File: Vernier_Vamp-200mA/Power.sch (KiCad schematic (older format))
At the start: 69 parts, among them J4 Conn_02x07_Odd_Even, Q1 Si4447ADY, Q2 IRF8707PbF, SW1 DPDT_Hirose, U1 LM4040DBZ-5, U2 LM4040DBZ-5, U3 LM393, U4 TPS7A470x, U5 TPS7A470x, U6 TPS7A33

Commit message: Coil driver version 1.0B
Updated coil driver 200mA version with fixes requested by Iain.
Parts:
- removed C56, C57, C58, C59, C62, C63: 100n, Capacitor_SMD:C_0603_1608Metric_Pad1.05x0.95mm_HandSolder, symbol Device:C_Small
- removed D3, D4, D5, D6: SMBJ16A, Diode_SMD:D_SMB_Handsoldering, symbol SMBJ15A:SMBJ15A
- removed F1, F2: 1A, Fuse:Fuse_1812_4532Metric_Pad1.30x3.40mm_HandSolder, symbol Device:Polyfuse_Small
- removed H1, H2, H3, H4, H5: MountingHole_Pad, MountingHole:MountingHole_3.2mm_M3_Pad_Via, symbol Mechanical:MountingHole_Pad
- removed J4: Conn_02x07_Odd_Even, Connector_Hirose:Hirose_DF11-14DP-2DSA_2x07_P2.00mm_Vertical, symbol Connector_Generic:Conn_02x07_Odd_Even
- removed Q1: Si4447ADY, Package_SO:SO-8_3.9x4.9mm_P1.27mm, symbol Si4447ADY:Si4447ADY
- removed Q2: IRF8707PbF, Package_SO:SO-8_3.9x4.9mm_P1.27mm, symbol IRF8707PbF:IRF8707PbF
- removed R1, R11, R12, R15, R16, R17, R2, R3, R4, R5, R6: 10k, Resistor_SMD:R_0603_1608Metric_Pad1.05x0.95mm_HandSolder, symbol Device:R_Small
- removed R10, R8: 100k, Resistor_SMD:R_0603_1608Metric_Pad1.05x0.95mm_HandSolder, symbol Device:R_Small
- removed R7, R9: 120k, Resistor_SMD:R_0603_1608Metric_Pad1.05x0.95mm_HandSolder, symbol Device:R_Small
- removed SW1: DPDT_Hirose, Connector_Hirose:Hirose_DF11-6DP-2DSA_2x03_P2.00mm_Vertical, symbol SW_DPDT_Hirose:DPDT_Hirose
- removed TP1, TP10, TP11, TP2, TP3, TP4, TP5, TP6, TP7, TP8, TP9: TestPoint_Probe, TestPoint:TestPoint_Pad_D1.0mm, symbol Connector:TestPoint_Probe
- removed U1, U2: LM4040DBZ-5, Package_TO_SOT_SMD:SOT-23, symbol Reference_Voltage:LM4040DBZ-5
- removed U3: LM393, Package_SO:TSSOP-8_4.4x3mm_P0.65mm, symbol Comparator:LM393
- U4, U5: symbol TPS74A4700:TPS7A470x -> TPS74A4700:TPS7A4700
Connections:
- net labels added: +7.5V, -7.5V
- net labels removed: +5VD, +5V_c_ref, +8V, +BATT, -5V_c_ref, -8V, -BATT, LED1_N, LED1_P, LED2_N, LED2_P, LED3_N, LED3_P, LED4_N, LED4_P, LED5_N, LED5_P, LED6_N, LED6_P, LED7_N, LED7_P
- wire segments 254 -> 100
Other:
- note added: "Ultra low noise LDO, configured to provide +7.5VDC"
- note added: "Ultra low noise LDO, configured to provide\n -7.5VDC\nComplementary pair to TPS7A470x"
- note removed: "Extra redundancy passive protection\nLimits the supply to 16.7V\nUses PPTC as a resetable fuse"
- note removed: "Low battery indicator (< 11V)\n"
- note removed: "Panel LED\nconnector"
- note removed: "Positive/Negative active protection\ncircuit\nTVS used to limit GS voltage\nalso used for ESD protection"
- note removed: "Power good\nindicators"
- note removed: "Reverse polarity protection\n"
- note removed: "Soft On/Off DPDT switch\n"
- note removed: "Ultra low noise LDO, configured to provide +7.5VDC (ignore +8V label)"
- note removed: "Ultra low noise LDO, configured to provide\n -7.5VDC (ignore -8V label)\nComplementary pair to TPS7A470x"
- moved on the sheet: C10, C11, C12, C13, C4, C5, C6, C7, C8, C9, NT1, R13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

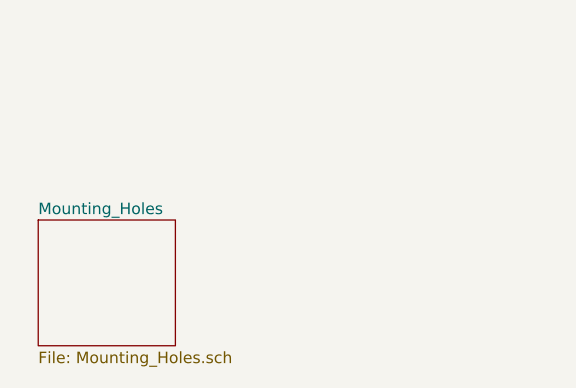
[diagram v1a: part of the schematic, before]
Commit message: Schematic and layout changes
Schematic updates:
- Added extra comments
- Added description (BNC channels)
- Moved mounting holes to the title block
- Added an option for connecting low battery indicatior LEDs to either +12V or GND (Comparator pulls to -12V)
- Added a 0R resistor for connecting +12V to Vin of nano
Layout:
- Added board ID and datecode on both sides
- Fixed priority of GND copper islands that were causing issues
- Changed the ground plane to be solid on the connection point (still not ideal but better)
- All components with thermal vias require tented vias so left as default
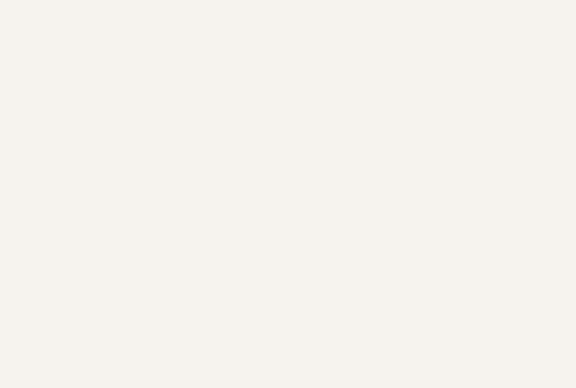
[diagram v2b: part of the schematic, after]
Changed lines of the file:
@@
 Connection ~ 7300 5350
-$Sheet
-S 600  7050 600  550
-U 5EA8762C
-F0 "Mounting_Holes" 50
-F1 "Mounting_Holes.sch" 50
-$EndSheet
 $Sheet
 S 1250 850  1450 750

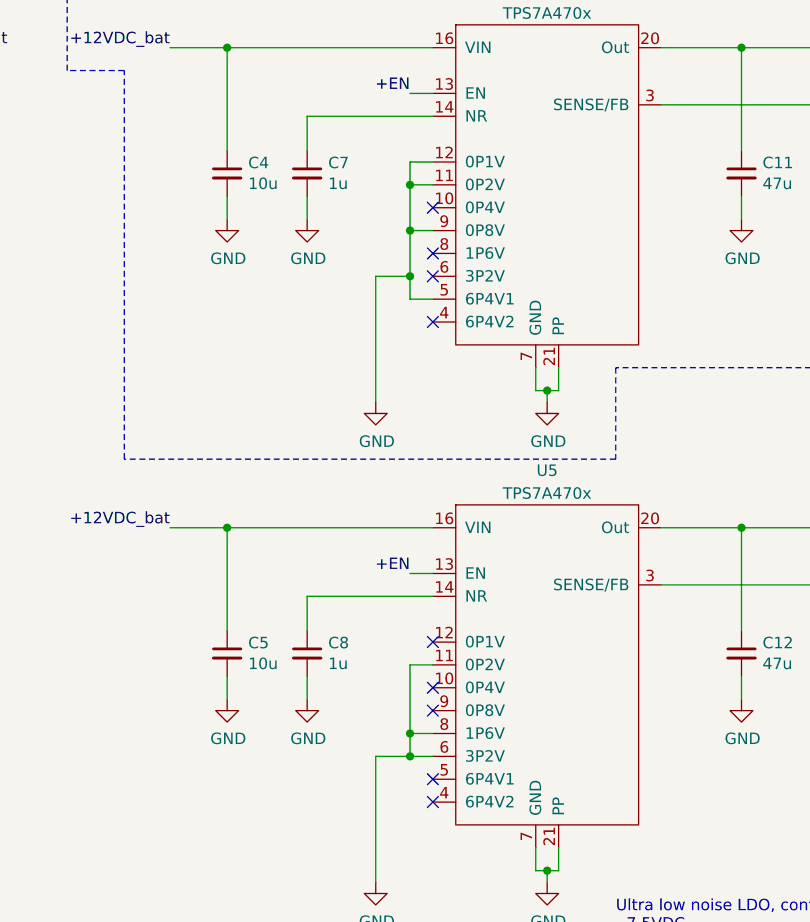
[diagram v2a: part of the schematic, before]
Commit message: 2 mA changes
-2 mA version is now called "low current coil driver" LCCD
- Small changes to the PCB layout
- Shield footprint correction
- General optimisation
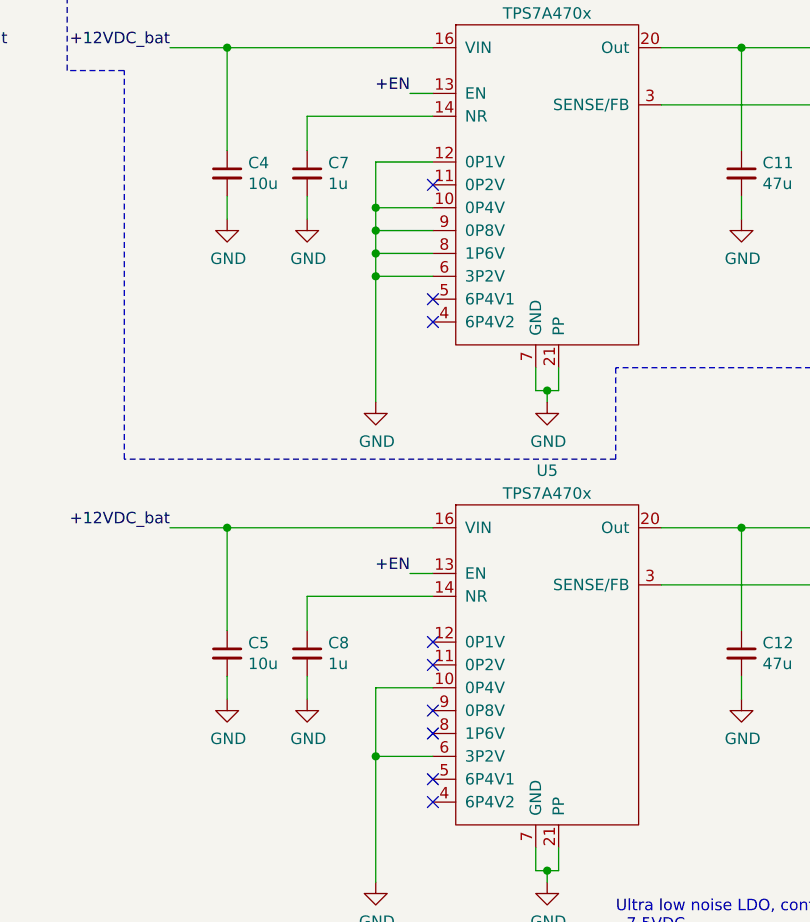
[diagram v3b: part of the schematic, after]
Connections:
- net GND: now also U4.10 (0P4V), U4.6 (3P2V), U4.8 (1P6V), U5.10 (0P4V); no longer U4.11 (0P2V), U4.5 (6P4V1), U5.11 (0P2V), U5.8 (1P6V)
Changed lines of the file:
@@
 Comment4 ""
 $EndDescr
-Wire Wire Line
-	5150 2150 5050 2150
-Wire Wire Line
-	5050 2050 5050 2150
 $Comp
 L power:GND #PWR0101
@@
 Wire Wire Line
 	4600 1700 4600 1800
-Connection ~ 5050 2050
-Wire Wire Line
-	5050 2050 4900 2050
-Wire Wire Line
-	4900 2050 4900 2600
 NoConn ~ 5150 2250
-NoConn ~ 5150 1950
 $Comp
 L Device:C_Small C4
@@
 Connection ~ 6500 1050
 Wire Wire Line
-	5150 4150 5050 4150
+	5150 4150 4900 4150
 $Comp
 L power:GND #PWR0122
@@
 Wire Wire Line
 	4600 3800 4600 3900
-Connection ~ 5050 4150
-Wire Wire Line
-	5050 4150 4900 4150
+Connection ~ 4900 4150
 Wire Wire Line
 	4900 4150 4900 4700
@@
 	6150 3400 7000 3400
 Connection ~ 6500 3150
-NoConn ~ 5150 3850
-Wire Wire Line
-	5150 4050 5050 4050
-Wire Wire Line
-	5050 4050 5050 4150
-Wire Wire Line
-	5150 3750 5050 3750
-Wire Wire Line
-	5050 3750 5050 4050
-Connection ~ 5050 4050
+NoConn ~ 5150 3750
 NoConn ~ 5150 4250
 Text Label 5050 1250 2    50   ~ 0
@@
 Wire Wire Line
 	4250 3150 5150 3150
-NoConn ~ 5150 2050
-NoConn ~ 5150 1750
-Wire Wire Line
-	5150 1550 5050 1550
-Wire Wire Line
-	5050 1550 5050 1650
-Wire Wire Line
-	5150 1650 5050 1650
-Connection ~ 5050 1650
-Wire Wire Line
-	5050 1650 5050 1850
-Wire Wire Line
-	5150 1850 5050 1850
-Connection ~ 5050 1850
-Wire Wire Line
-	5050 1850 5050 2050
+NoConn ~ 5150 2150
+NoConn ~ 5150 1650
 Text Notes 5300 7600 0    50   ~ 0
 Star ground point\n
@@
 	1    0    0    -1
 $EndComp
+Wire Wire Line
+	5150 1550 4900 1550
+Wire Wire Line
+	4900 1550 4900 1750
+Wire Wire Line
+	5150 1750 4900 1750
+Connection ~ 4900 1750
+Wire Wire Line
+	4900 1750 4900 1850
+Wire Wire Line
+	5150 1850 4900 1850
+Connection ~ 4900 1850
+Wire Wire Line
+	4900 1850 4900 1950
+Wire Wire Line
+	5150 1950 4900 1950
+Connection ~ 4900 1950
+Wire Wire Line
+	4900 1950 4900 2050
+Wire Wire Line
+	5150 2050 4900 2050
+Connection ~ 4900 2050
+Wire Wire Line
+	4900 2050 4900 2600
+NoConn ~ 5150 4050
+Wire Wire Line
+	4900 3850 5150 3850
+Wire Wire Line
+	4900 3850 4900 4150
 $EndSCHEMATC
